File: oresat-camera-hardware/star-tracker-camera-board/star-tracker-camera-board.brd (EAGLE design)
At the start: 31.5 x 14 mm, 46 parts, among them J1 3-1734742-6, U1 AR0134CSSM00SPCA0, U2 TPS70618DRVR, U3 TPS71928-28DRVT, U4 TPS71928-28DRVT, X1 KC2520B27.0000C10E00

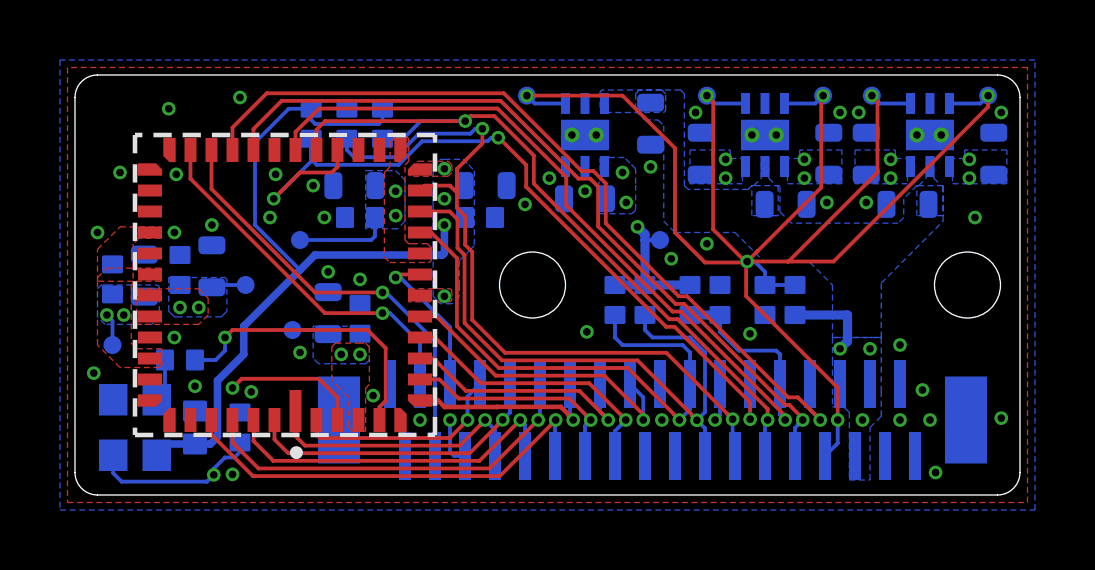
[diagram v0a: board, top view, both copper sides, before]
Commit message: updated the star tracker camera board with smaller dimensions
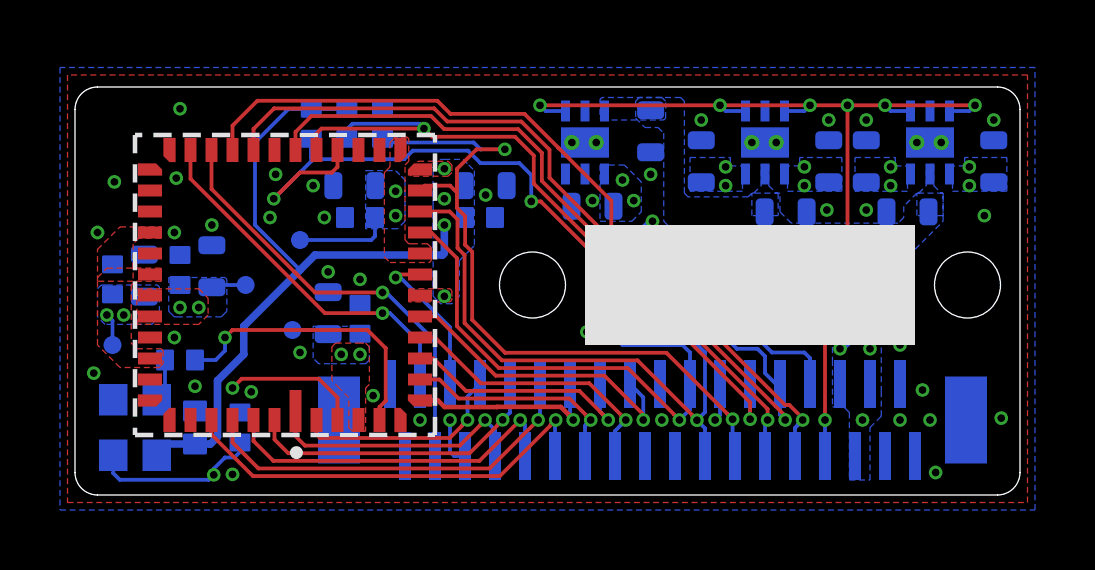
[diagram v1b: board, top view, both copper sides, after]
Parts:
- removed TP1, TP2, TP3, TP4, TP5: TPTP06R, J-TestPoint-Small:TP06R
- moved R11 1.19 mm to (9.06, 12.4)
- moved R9 1.19 mm to (10.2, 12.4)
- moved TP8 0.49 mm to (19.8, 8.12)
- moved C19 0.35 mm to (17.2, 9.62)
- moved C10 0.25 mm to (27.8, 9.44)
- moved C11 0.25 mm to (30.6, 11.1)
- moved C14 0.25 mm to (19.2, 12.1)
- moved C15 0.25 mm to (25.1, 11.1)
- moved C18 0.25 mm to (20.9, 11.1)
- moved C6 0.25 mm to (23.7, 9.44)
- moved C7 0.25 mm to (26.4, 11.1)
- moved R5 0.25 mm to (24.2, 6.50)
- moved R6 0.25 mm to (23.2, 6.50)
- moved U2 0.25 mm to (17.0, 11.8)
- moved U3 0.25 mm to (23.0, 11.8)
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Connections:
- net VREG_EN: no longer TP1.TP, TP2.TP, TP3.TP, TP4.TP, TP5.TP
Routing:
- net VREG_EN: track 58.4 -> 35.4 mm, vias 7 -> 8
- net TRIGGER: track 27.4 -> 25.4 mm
- net VDD_IO: track 42.0 -> 40.3 mm
- net !RESET: track 25.0 -> 24.0 mm
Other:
- board size 31.5 x 14 mm -> 31.5 x 13.6 mm
- board text added: "OCBv4 OLIVER REW 2020.10.19"
- board text removed: "OCBv3 OLIVER REW 2020.05.31"
